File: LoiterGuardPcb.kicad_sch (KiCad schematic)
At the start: 0 parts

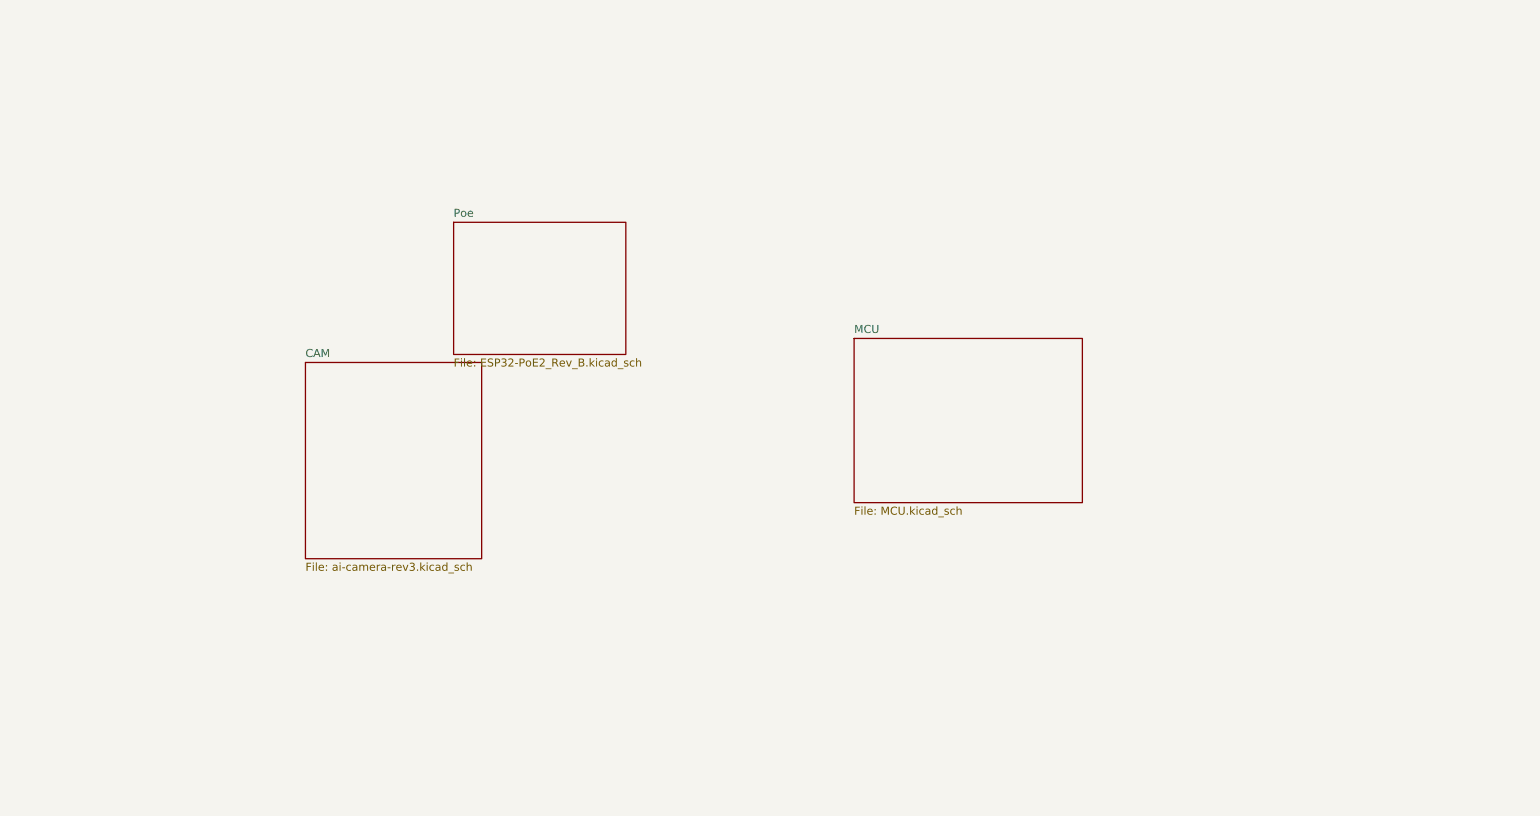
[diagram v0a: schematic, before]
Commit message: updated poe schematic
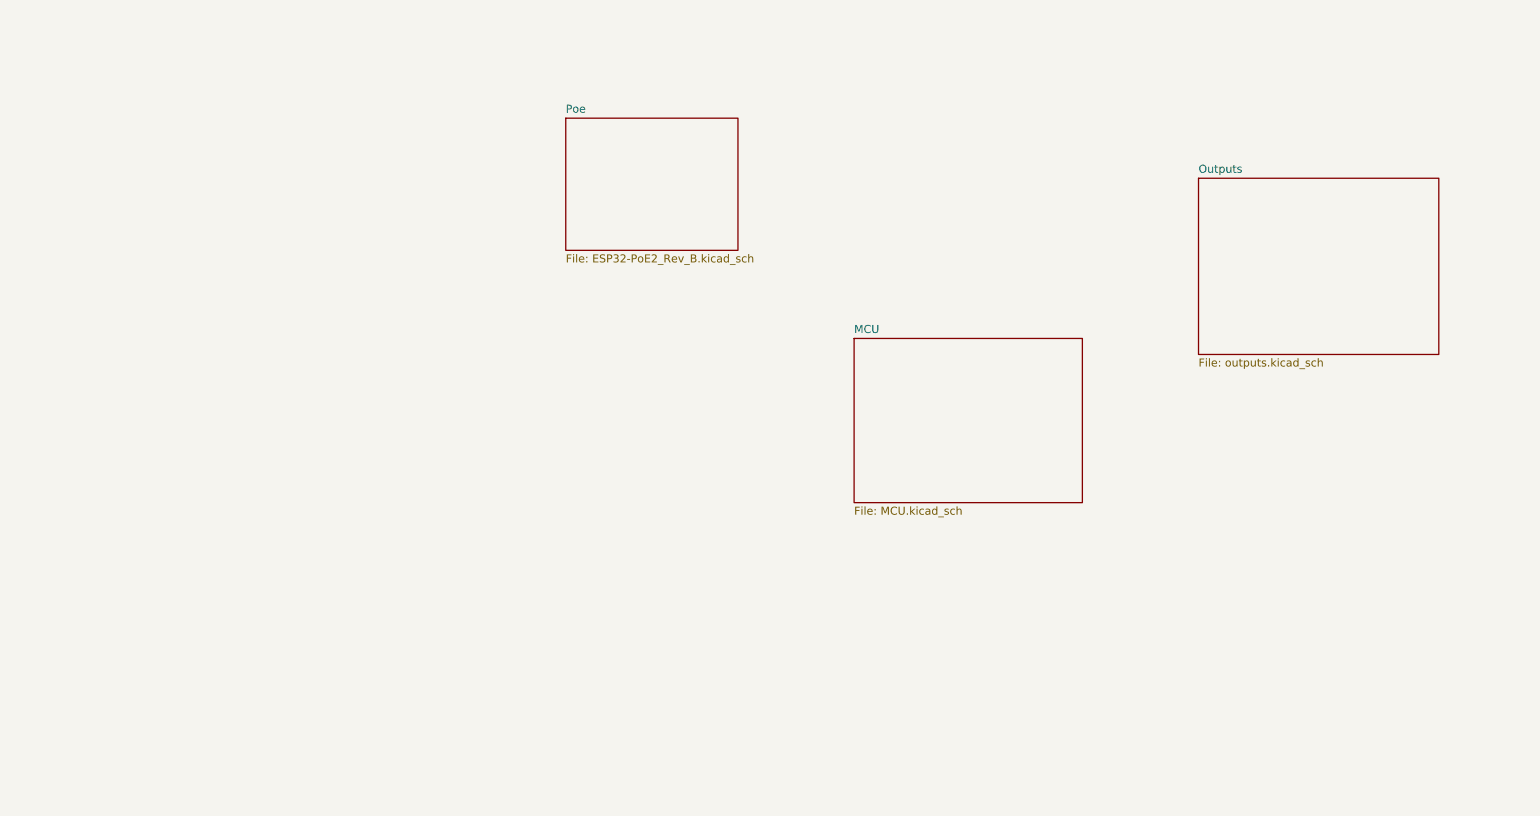
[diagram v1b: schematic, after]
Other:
- removed sheet CAM
- added sheet Outputs (outputs.kicad_sch)
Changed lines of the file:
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@@
 	(paper "A4")
+	(sheet
+		(at 209.55 59.055)
+		(size 38.1 27.94)
+		(exclude_from_sim no)
+		(in_bom yes)
+		(on_board yes)
+		(dnp no)
+		(fields_autoplaced yes)
+		(stroke
+			(width 0.1524)
+			(type solid)
+		)
+		(fill
+			(color 0 0 0 0.0000)
+		)
+		(property "Sheetname" "Outputs"
+			(at 209.55 58.3434 0)
+			(effects
+				(font
+					(size 1.27 1.27)
+				)
+				(justify left bottom)
+			)
+		)
+		(property "Sheetfile" "outputs.kicad_sch"
+			(at 209.55 87.5796 0)
+			(effects
+				(font
+					(size 1.27 1.27)
+				)
+				(justify left top)
+			)
+		)
+		(instances
+			(project "LoiterGuardPcb"
+				(path "/e0fc1b62-e519-47f0-a0fc-4ac6dbab9b04"
+					(page "5")
+				)
+			)
+		)
+	)
 	(sheet
 		(at 154.94 84.455)
@@
 	)
 	(sheet
-		(at 67.945 88.265)
-		(size 27.94 31.115)
-		(exclude_from_sim no)
-		(in_bom yes)
-		(on_board yes)
-		(dnp no)
-		(fields_autoplaced yes)
-		(stroke
-			(width 0.1524)
-			(type solid)
-		)
-		(fill
-			(color 0 0 0 0.0000)
-		)
-		(property "Sheetname" "CAM"
-			(at 67.945 87.5534 0)
-			(effects
-				(font
-					(size 1.27 1.27)
-				)
-				(justify left bottom)
-			)
-		)
-		(property "Sheetfile" "ai-camera-rev3.kicad_sch"
-			(at 67.945 119.9646 0)
-			(effects
-				(font
-					(size 1.27 1.27)
-				)
-				(justify left top)
-			)
-		)
-		(instances
-			(project "LoiterGuardPcb"
-				(path "/e0fc1b62-e519-47f0-a0fc-4ac6dbab9b04"
-					(page "4")
-				)
-			)
-		)
-	)
-	(sheet
-		(at 91.44 66.04)
+		(at 109.22 49.53)
 		(size 27.305 20.955)
 		(exclude_from_sim no)
@@
 		)
 		(property "Sheetname" "Poe"
-			(at 91.44 65.3284 0)
+			(at 109.22 48.8184 0)
 			(effects
 				(font
@@
 		)
 		(property "Sheetfile" "ESP32-PoE2_Rev_B.kicad_sch"
-			(at 91.44 87.5796 0)
+			(at 109.22 71.0696 0)
 			(effects
 				(font

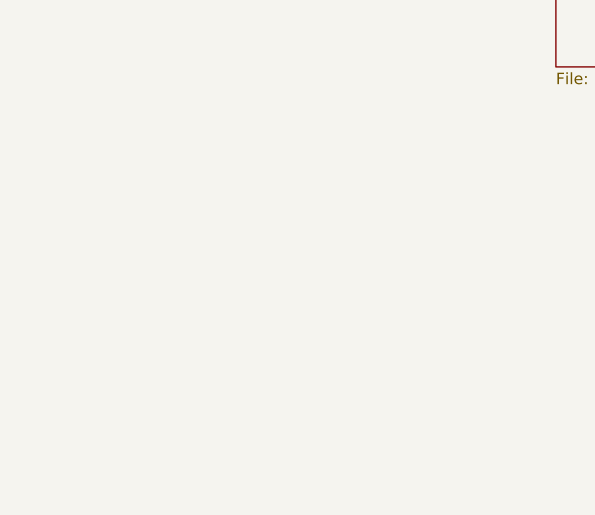
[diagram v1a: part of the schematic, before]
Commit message: GPIOs shouldn't have any conflicts
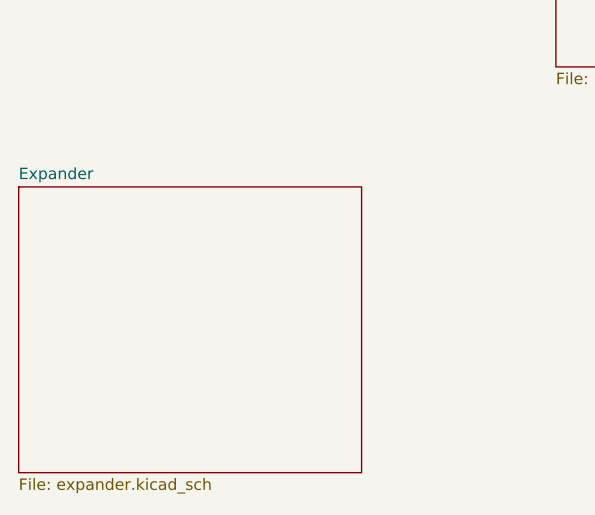
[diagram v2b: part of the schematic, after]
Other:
- added sheet Expander (expander.kicad_sch)
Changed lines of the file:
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@@
+	)
+	(sheet
+		(at 95.25 123.825)
+		(size 38.1 31.75)
+		(exclude_from_sim no)
+		(in_bom yes)
+		(on_board yes)
+		(dnp no)
+		(fields_autoplaced yes)
+		(stroke
+			(width 0.1524)
+			(type solid)
+		)
+		(fill
+			(color 0 0 0 0.0000)
+		)
+		(property "Sheetname" "Expander"
+			(at 95.25 123.1134 0)
+			(effects
+				(font
+					(size 1.27 1.27)
+				)
+				(justify left bottom)
+			)
+		)
+		(property "Sheetfile" "expander.kicad_sch"
+			(at 95.25 156.1596 0)
+			(effects
+				(font
+					(size 1.27 1.27)
+				)
+				(justify left top)
+			)
+		)
+		(property "Field2" ""
+			(at 95.25 123.825 0)
+			(effects
+				(font
+					(size 1.27 1.27)
+				)
+			)
+		)
+		(instances
+			(project "LoiterGuardPcb"
+				(path "/e0fc1b62-e519-47f0-a0fc-4ac6dbab9b04"
+					(page "5")
+				)
+			)
+		)
 	)
 	(sheet

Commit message: wip - started traces for layout
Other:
- sheet Expander ports: added CAM_SD_MISO, CAM_SD_MOSI, CAM_SD_SCLK, CELL_ON_OFF, CELL_RST, CELL_STATUS, DF_BUSY, ETH_RST, MM_SOP, MM_SYNC, SCL, SDA, SPARE1, SPARE2, WD_DONE, ~{IO_RST}, ~{MM_RST}, ~{SD_CS}; removed none
- sheet MCU ports: added BUZZ/USB-, CAM_SD_MISO, CAM_SD_MOSI, CAM_SD_SCLK, CELL_ON_OFF, CELL_RST, CELL_STATUS, DF_RX, DF_TX, ETH_MISO, ETH_MOSI, ETH_SCLK, LED1, LED2, LED3, MM_CTS, MM_RTS, MM_RX, MM_TX, SCL, SDA, STROBE/USB+, WD_DONE, ~{CAM_CS}, ~{ETH_CS}, ~{ETH_INT}, ~{IO_RST}, ~{SD_CS}; removed none
- sheet Outputs ports: added BUZZ/USB-, CAM_SD_MISO, CAM_SD_MOSI, CAM_SD_SCLK, DF_BUSY, DF_RX, DF_TX, LED1, LED2, LED3, MM_CTS, MM_RTS, MM_RX, MM_SOP, MM_SYNC, MM_TX, SPARE1, SPARE2, STROBE/USB+, ~{CAM_CS}, ~{MM_RST}; removed none
- sheet Poe ports: added ETH_MISO, ETH_MOSI, ETH_SCLK, ~{ETH_CS}, ~{ETH_INT}, ~{ETH_RST}; removed none
